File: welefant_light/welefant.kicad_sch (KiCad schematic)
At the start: 75 parts, among them J1 Conn_01x02, J2 Conn_02x8_Odd_Even, J3 Conn_02x11_Odd_Even, Q1 AO3401A, Q2 AO3401A, Q3 AO3401A, SW1 DPDT, SW2 RESET, SW3 BOOT, U1 NCP167BMX330TBG, U2 Audio Jack PJ-324, U3 GSA4737H12-F26-6P, U4 TP4056, U5 welefant, U6 ESP32-S3-WROOM-1(N16R2)

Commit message: blubb
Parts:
- removed D4: SS34, easyeda2kicad:SMA_L4.3-W2.6-LS5.2-RD, symbol easyeda2kicad:SS34_C8678
- removed R11: 2.4K, easyeda2kicad:R0603, symbol easyeda2kicad:0603WAF2401T5E
- added D4: 1N5819WS, Diode_SMD:D_SOD-323, symbol Diode:1N5819WS
- added R18: 10K, easyeda2kicad:R0603, symbol easyeda2kicad:0603WAF1002T5E
- added R19: 330, easyeda2kicad:R0603, symbol easyeda2kicad:0603WAF3300T5E
- BT1: value Battery_Cell -> Battery
- J1: footprint Connector_JST:JST_PH_B2B-PH-SM4-TB_1x02-1MP_P2.00mm_Vertical -> Connector_JST:JST_PH_B2B-PH-K_1x02_P2.00mm_Vertical
- J2, J3: footprint Connector_PinHeader_2.54mm:PinHeader_2x08_P2.54mm_Vertical_SMD -> hacrafu:PinHeader_2x08_P2.54mm_Vertical_SMD_handsolder
- SW1: footprint footprints:Switch_MSS22D18 -> hacrafu:Switch_MSS22D18
- U1: footprint easyeda2kicad:XDFN-4_L1.0-W1.0-P0.65-BL-EP -> hacrafu:XDFN-4
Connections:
- net BAT_SENS_EN: now also R18.2
- net GND: now also C11.2, SW2.4 (D), SW3.3 (C), U4.9 (EP)
- net V33: now also R18.1
- net V5: now also D4.2 (A)
- net VBUS: now also D4.1 (K)
- net at CLED1.1 (C): now also R19.1
- net at U4.7 (~{CHRG}): now also R19.2
- net RESET: now reaches C11.1, R17.2, SW2.2 (B), U6.3 (EN)
- net RESET: now also SW2.1 (A)
- net IO0: now reaches SW3.1 (A), U6.27 (IO0)
- net IO0: now also SW3.2 (B)
- no-connect marks 21 -> 17
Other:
- moved on the sheet: R16, SW3

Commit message: stand
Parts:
- BT1: footprint hacrafu:LiPo_Recycled -> hacrafu:LiPo_Recycled_welefant
- J3: value Conn_02x11_Odd_Even -> Conn_02x6_Odd_Even; footprint hacrafu:PinHeader_2x08_P2.54mm_Vertical_SMD_handsolder -> hacrafu:PinHeader_2x06_P2.54mm_Vertical_SMD_handsolder; symbol Connector_Generic:Conn_02x08_Odd_Even -> Connector_Generic:Conn_02x06_Odd_Even
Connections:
- net IO35: now also J3.5 (Pin_5); no longer J3.9 (Pin_9)
- net IO36: now also J3.6 (Pin_6); no longer J3.10 (Pin_10)
- net IO37: now also J3.7 (Pin_7); no longer J3.11 (Pin_11)
- net IO38: now also J3.8 (Pin_8); no longer J3.12 (Pin_12)
- net IO39: now also J3.9 (Pin_9); no longer J3.13 (Pin_13)
- net IO40: now also J3.10 (Pin_10); no longer J3.14 (Pin_14)
- net IO41: now also J3.11 (Pin_11); no longer J3.15 (Pin_15)
- net IO42: now also J3.12 (Pin_12); no longer J3.16 (Pin_16)
- net TOUCH_T4: no longer J3.5 (Pin_5)
- net TOUCH_T5: no longer J3.6 (Pin_6)
- net TOUCH_T6: no longer J3.7 (Pin_7)
- net IO21: no longer names the net of U6.23 (IO21)
- net IO21: no longer J3.8 (Pin_8)
- no-connect marks 17 -> 18
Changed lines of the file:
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@@
   (no_connect (at 183.515 38.1))
   (no_connect (at 27.94 25.4))
+  (no_connect (at 251.46 78.74))
   (no_connect (at 38.1 13.97))
   (no_connect (at 259.08 78.74))
@@
     (effects (font (size 1.27 1.27)) (justify right bottom))
   )
-  (label "IO21" (at 270.51 114.3 0) (fields_autoplaced)
-    (effects (font (size 1.27 1.27)) (justify left bottom))
-  )
   (label "LED_HEAD" (at 254 78.74 270) (fields_autoplaced)
     (effects (font (size 1.27 1.27)) (justify right bottom))
@@
     (effects (font (size 1.27 1.27)) (justify right bottom))
   )
-  (label "IO35" (at 257.81 116.84 180) (fields_autoplaced)
+  (label "IO35" (at 257.81 111.76 180) (fields_autoplaced)
     (effects (font (size 1.27 1.27)) (justify right bottom))
   )
@@
     (effects (font (size 1.27 1.27)) (justify right bottom))
   )
-  (label "TOUCH_T6" (at 257.81 114.3 180) (fields_autoplaced)
-    (effects (font (size 1.27 1.27)) (justify right bottom))
-  )
-  (label "IO36" (at 270.51 116.84 0) (fields_autoplaced)
+  (label "IO36" (at 270.51 111.76 0) (fields_autoplaced)
     (effects (font (size 1.27 1.27)) (justify left bottom))
   )
@@
     (effects (font (size 1.27 1.27)) (justify right bottom))
   )
-  (label "TOUCH_T4" (at 257.81 111.76 180) (fields_autoplaced)
-    (effects (font (size 1.27 1.27)) (justify right bottom))
-  )
   (label "TX" (at 220.345 109.22 0) (fields_autoplaced)
     (effects (font (size 1.27 1.27)) (justify left bottom))
@@
     (effects (font (size 1.27 1.27)) (justify left bottom))
   )
-  (label "IO38" (at 270.51 119.38 0) (fields_autoplaced)
+  (label "IO38" (at 270.51 114.3 0) (fields_autoplaced)
     (effects (font (size 1.27 1.27)) (justify left bottom))
   )
@@
     (effects (font (size 1.27 1.27)) (justify right bottom))
   )
-  (label "IO41" (at 257.81 124.46 180) (fields_autoplaced)
+  (label "IO41" (at 257.81 119.38 180) (fields_autoplaced)
     (effects (font (size 1.27 1.27)) (justify right bottom))
   )
@@
     (effects (font (size 1.27 1.27)) (justify right bottom))
   )
-  (label "IO39" (at 257.81 121.92 180) (fields_autoplaced)
-    (effects (font (size 1.27 1.27)) (justify right bottom))
-  )
-  (label "IO21" (at 251.46 78.74 270) (fields_autoplaced)
+  (label "IO39" (at 257.81 116.84 180) (fields_autoplaced)
     (effects (font (size 1.27 1.27)) (justify right bottom))
   )
@@
     (effects (font (size 1.27 1.27)) (justify left bottom))
   )
-  (label "IO42" (at 270.51 124.46 0) (fields_autoplaced)
+  (label "IO42" (at 270.51 119.38 0) (fields_autoplaced)
     (effects (font (size 1.27 1.27)) (justify left bottom))
   )
@@
     (effects (font (size 1.27 1.27)) (justify right bottom))
   )
-  (label "TOUCH_T5" (at 270.51 111.76 0) (fields_autoplaced)
-    (effects (font (size 1.27 1.27)) (justify left bottom))
-  )
   (label "VEXT" (at 49.53 152.4 0) (fields_autoplaced)
     (effects (font (size 1.27 1.27)) (justify left bottom))
@@
     (effects (font (size 1.27 1.27)) (justify right bottom))
   )
-  (label "IO40" (at 270.51 121.92 0) (fields_autoplaced)
+  (label "IO40" (at 270.51 116.84 0) (fields_autoplaced)
     (effects (font (size 1.27 1.27)) (justify left bottom))
   )
@@
     (effects (font (size 1.27 1.27)) (justify left bottom))
   )
-  (label "IO37" (at 257.81 119.38 180) (fields_autoplaced)
+  (label "IO37" (at 257.81 114.3 180) (fields_autoplaced)
     (effects (font (size 1.27 1.27)) (justify right bottom))
   )
@@
     )
   )
-  (symbol (lib_id "Connector_Generic:Conn_02x08_Odd_Even") (at 262.89 114.3 0) (unit 1)
+  (symbol (lib_id "Connector_Generic:Conn_02x06_Odd_Even") (at 262.89 111.76 0) (unit 1)
     (in_bom yes) (on_board yes) (dnp no)
-    (property "Reference" "J3" (at 264.795 100.33 0)
-      (effects (font (size 1.27 1.27)))
-    )
-    (property "Value" "Conn_02x11_Odd_Even" (at 264.16 102.87 0)
-      (effects (font (size 1.27 1.27)))
-    )
-    (property "Footprint" "hacrafu:PinHeader_2x08_P2.54mm_Vertical_SMD_handsolder" (at 262.89 114.3 0)
-      (effects (font (size 1.27 1.27)) hide)
-    )
-    (property "Datasheet" "~" (at 262.89 114.3 0)
+    (property "Reference" "J3" (at 264.795 100.965 0)
+      (effects (font (size 1.27 1.27)))
+    )
+    (property "Value" "Conn_02x6_Odd_Even" (at 264.16 102.87 0)
+      (effects (font (size 1.27 1.27)))
+    )
+    (property "Footprint" "hacrafu:PinHeader_2x06_P2.54mm_Vertical_SMD_handsolder" (at 262.89 111.76 0)
+      (effects (font (size 1.27 1.27)) hide)
+    )
+    (property "Datasheet" "~" (at 262.89 111.76 0)
       (effects (font (size 1.27 1.27)) hide)
     )
@@
     (pin "11")
     (pin "12")
-    (pin "13")
-    (pin "14")
-    (pin "15")
-    (pin "16")
     (pin "2")
     (pin "3")
@@
       (effects (font (size 1.27 1.27)) (justify left) hide)
     )
-    (property "Footprint" "hacrafu:LiPo_Recycled" (at 186.055 63.881 90)
-      (effects (font (size 1.27 1.27)) hide)
-    )
+    (property "Footprint" "hacrafu:LiPo_Recycled_welefant" (at 186.055 63.881 90)
+      (effects (font (size 1.27 1.27)) hide)
+    )

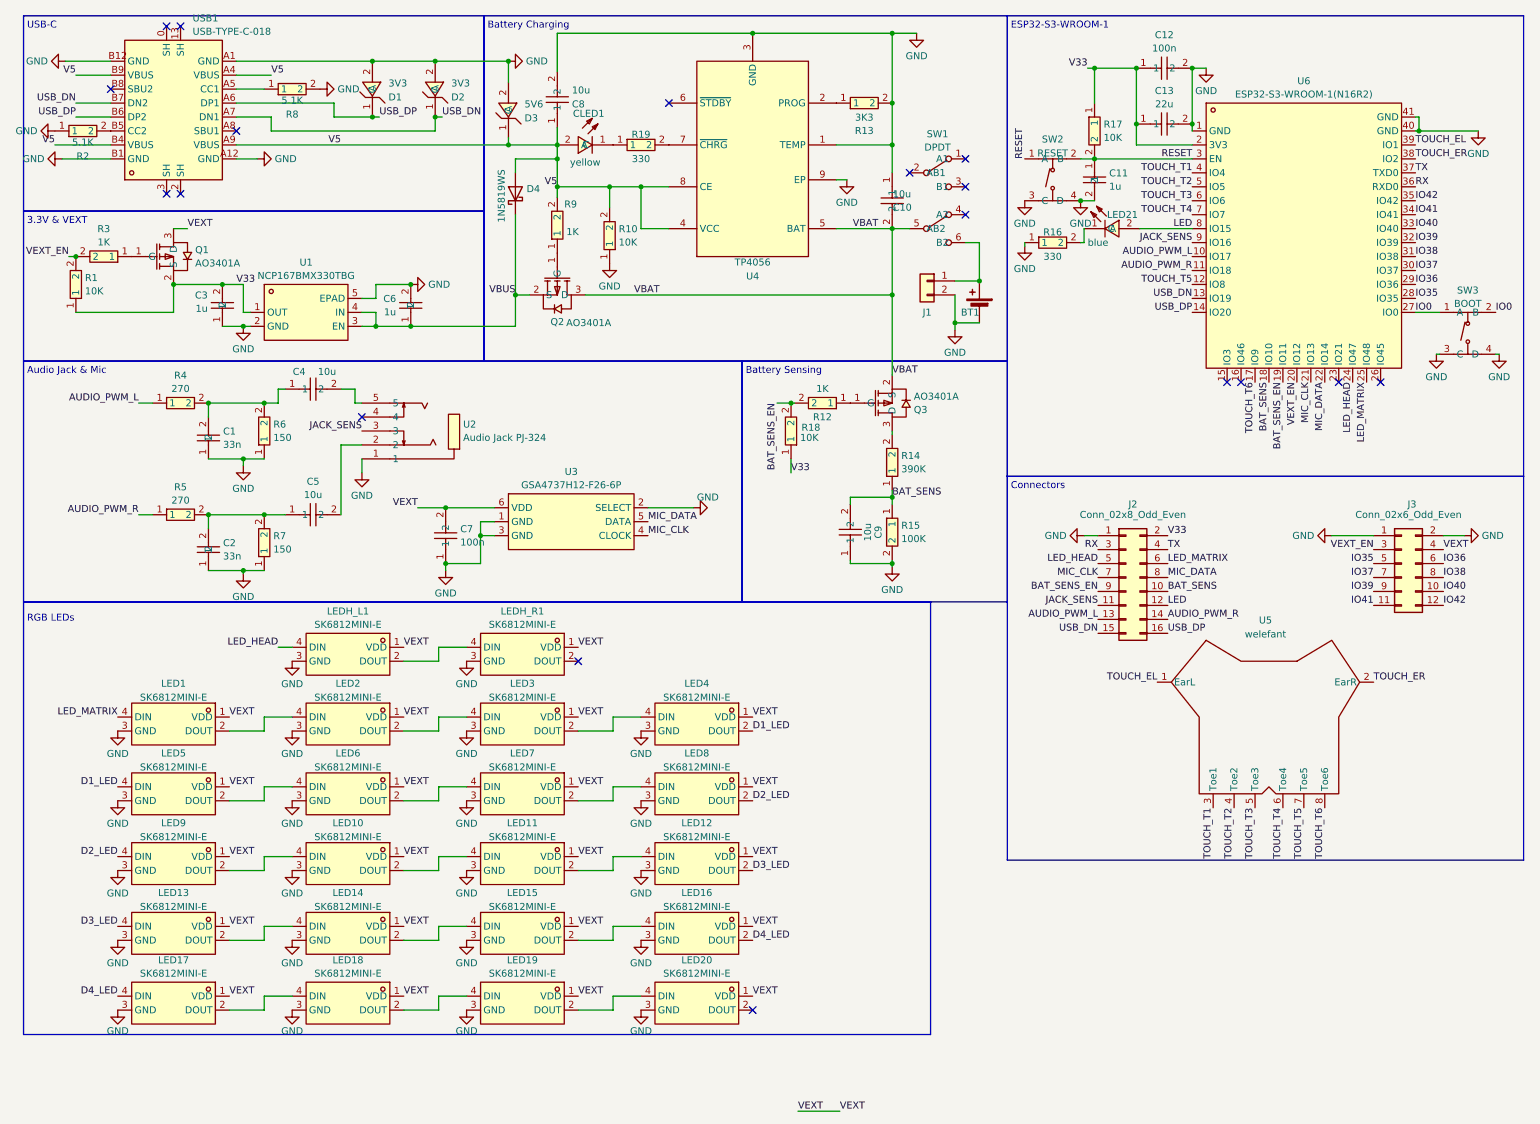
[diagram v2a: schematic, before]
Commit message: weiter welefant umgestaltung ohne wroom
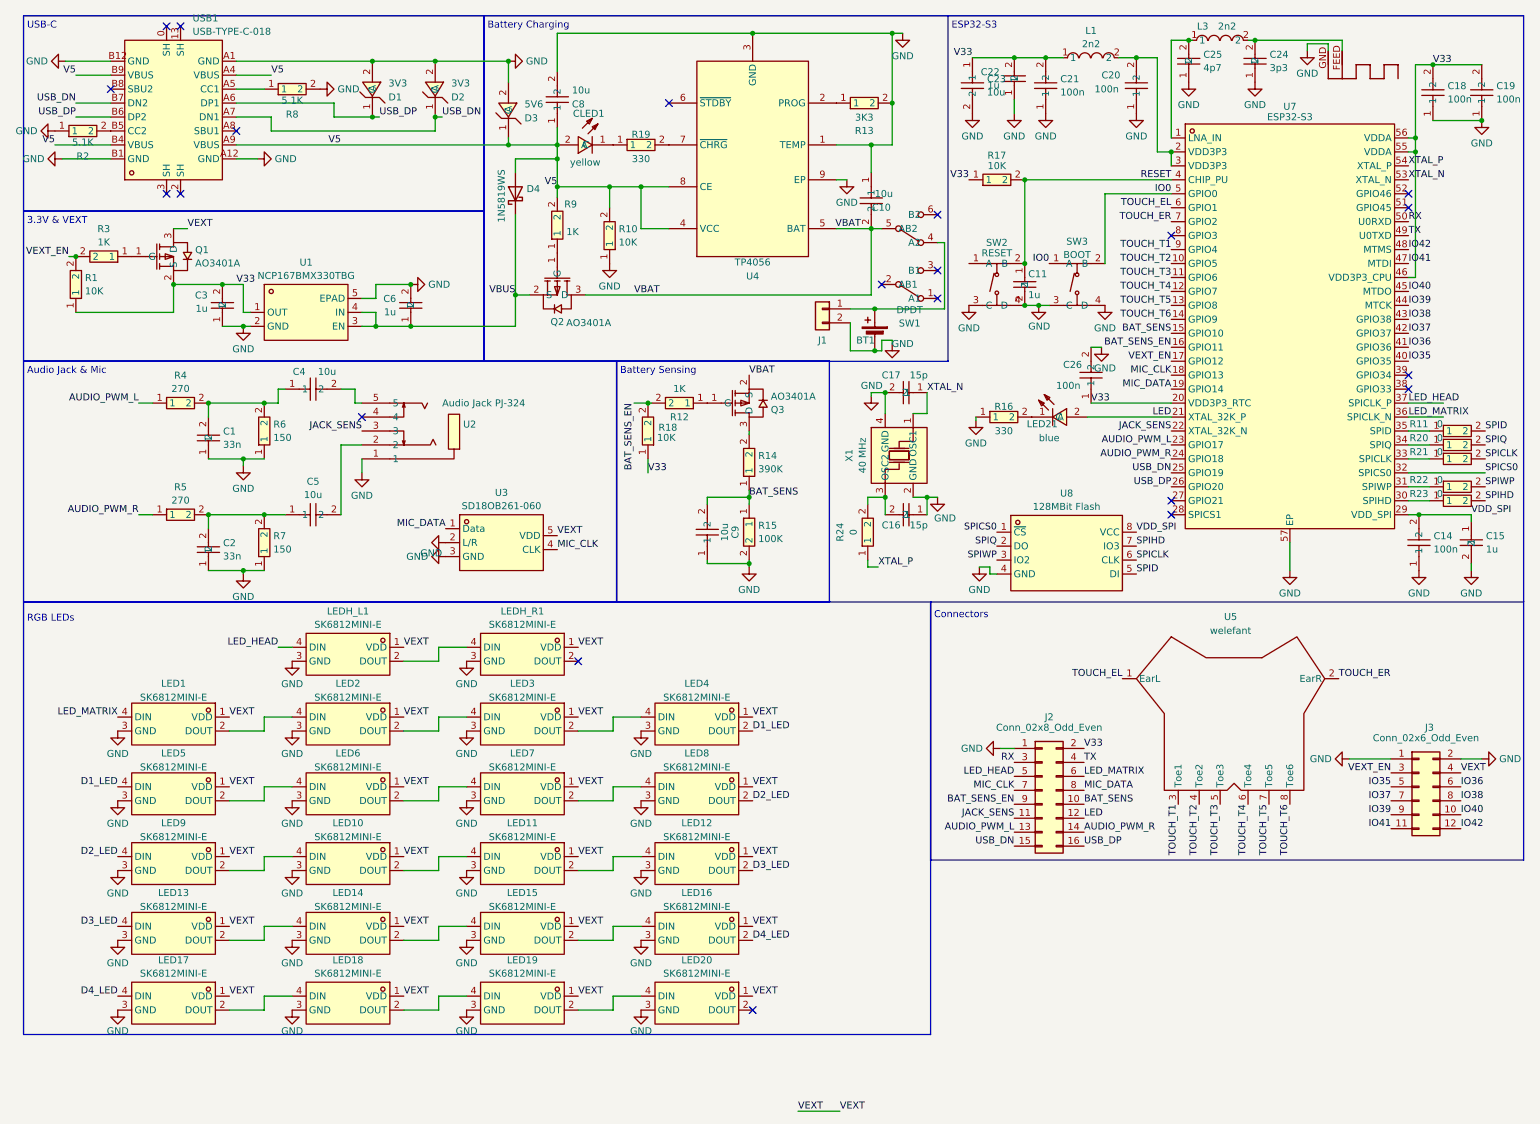
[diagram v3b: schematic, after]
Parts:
- removed C12, C7: 100n, easyeda2kicad:C0603, symbol easyeda2kicad:CC0603KRX7R9BB104
- removed C13: 22u, easyeda2kicad:C0603, symbol easyeda2kicad:CL10A226MQ8NRNC
- removed U3: GSA4737H12-F26-6P, easyeda2kicad:MIC-SMD_GSA4737H12-F26-6P, symbol easyeda2kicad:GSA4737H12-F26-6P
- removed U6: ESP32-S3-WROOM-1(N16R2), easyeda2kicad:WIRELM-SMD_ESP32-S3-WROOM-1, symbol easyeda2kicad:ESP32-S3-WROOM-1(N16R2)
- added ANT1: ANTENNA, hacrafu:antenna, symbol hacrafu:antenna
- added C14, C18, C19, C20, C21, C26: 100n, easyeda2kicad:C0603, symbol easyeda2kicad:CC0603KRX7R9BB104
- added C15, C22: 1u, easyeda2kicad:C0603, symbol easyeda2kicad:CL10A105KB8NNNC
- added C16, C17: 15p, easyeda2kicad:C0603, symbol easyeda2kicad:CL10C150JB8NNNC
- added C23: 10u, easyeda2kicad:C0603, symbol easyeda2kicad:CL10A106KP8NNNC
- added C24: 3p3, easyeda2kicad:C0402, symbol easyeda2kicad:0402CG3R3C500NT
- added C25: 4p7, easyeda2kicad:C0402, symbol easyeda2kicad:0402CG4R7C500NT
- added L1, L3: 2n2, easyeda2kicad:L0603, symbol easyeda2kicad:SDCL1608C2N2STDF
- added R11, R20, R21, R22, R23, R24: 0, easyeda2kicad:R0603, symbol easyeda2kicad:0603WAF0000T5E
- added U3: SD18OB261-060, easyeda2kicad:MIC-SMD_SD18OB261-060, symbol easyeda2kicad:SD18OB261-060
- added U7: ESP32-S3, easyeda2kicad:QFN-56_L7.0-W7.0-P0.40-TL-EP4.0, symbol easyeda2kicad:ESP32-S3
- added U8: 128MBit Flash, easyeda2kicad:SOIC-8_L5.3-W5.3-P1.27-LS8.0-BL, symbol easyeda2kicad:W25Q128JVSIQTR
- added X1: 40 MHz, easyeda2kicad:OSC-SMD_4P-L3.2-W2.5-BL_SIT8008BI, symbol easyeda2kicad:X322540MPB4SI
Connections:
- net AUDIO_PWM_L: now also U7.23 (GPIO17)
- net AUDIO_PWM_R: now also U7.24 (GPIO18)
- net BAT_SENS: now also U7.15 (GPIO10)
- net BAT_SENS_EN: now also U7.16 (GPIO11)
- net GND: now also ANT1.GND, C14.1, C15.2, C16.1, C17.2, C18.1, C19.1, C20.1, C21.1, C22.1, C23.2, C24.1, C25.1, C26.2, U3.2 (L/R), U3.3 (GND), U7.57 (EP), U8.4 (GND), X1.2 (GND), X1.4 (GND)
- net IO0: now also U7.5 (GPIO0)
- net IO35: now also U7.40 (GPIO35)
- net IO36: now also U7.41 (GPIO36)
- net IO37: now also U7.42 (GPIO37)
- net IO38: now also U7.43 (GPIO38)
- net IO39: now also U7.44 (MTCK)
- net IO40: now also U7.45 (MTDO)
- net IO41: now also U7.47 (MTDI)
- net IO42: now also U7.48 (MTMS)
- net JACK_SENS: now also U7.22 (XTAL_32K_N)
- net LED: now also U7.21 (XTAL_32K_P)
- net LED_HEAD: now also U7.37 (SPICLK_P)
- net LED_MATRIX: now also U7.36 (SPICLK_N)
- net MIC_CLK: now also U3.4 (CLK), U7.18 (GPIO13)
- net MIC_DATA: now also U3.1 (Data), U7.19 (GPIO14)
- net RESET: now also U7.4 (CHIP_PU); no longer SW2.1 (A)
- net RX: now also U7.50 (U0RXD)
- net TOUCH_EL: now also U7.6 (GPIO1)
- net TOUCH_ER: now also U7.7 (GPIO2)
- net TOUCH_T1: now also U7.9 (GPIO4)
- net TOUCH_T2: now also U7.10 (GPIO5)
- net TOUCH_T3: now also U7.11 (GPIO6)
- net TOUCH_T4: now also U7.12 (GPIO7)
- net TOUCH_T5: now also U7.13 (GPIO8)
- net TOUCH_T6: now also U7.14 (GPIO9)
- net TX: now also U7.49 (U0TXD)
- net USB_DN: now also U7.25 (GPIO19)
- net USB_DP: now also U7.26 (GPIO20)
- net V33: now also C18.2, C19.2, C21.2, C22.2, C23.1, C26.1, L1.1, U7.20 (VDD3P3_RTC), U7.46 (VDD3P3_CPU), U7.55 (VDDA), U7.56 (VDDA)
- net VEXT: now also U3.5 (VDD)
- net VEXT_EN: now also U7.17 (GPIO12)
- net at BT1.1 (+), J1.1 (Pin_1): now also SW1.4 (A2); no longer SW1.6 (B2)
- new net: C16.2, R24.2, X1.3 (OSC2)
- new net: R21.1, U7.33 (SPICLK)
- new net: C20.2, L1.2, U7.2 (VDD3P3), U7.3 (VDD3P3)
- new net: C25.2, L3.1, U7.1 (LNA_IN)
- new net: R23.1, U7.30 (SPIHD)
- new net: R22.1, U7.31 (SPIWP)
- new net: R20.1, U7.34 (SPIQ)
- new net: R11.1, U7.35 (SPID)
- new net: ANT1.FEED, C24.2, L3.2
- new net SPICLK: R21.2, U8.6 (CLK)
- new net SPICS0: U7.32 (SPICS0), U8.1 (~{CS})
- new net SPID: R11.2, U8.5 (DI)
- new net SPIHD: R23.2, U8.7 (IO3)
- new net SPIQ: R20.2, U8.2 (DO)
- new net SPIWP: R22.2, U8.3 (IO2)
- new net VDD_SPI: C14.2, C15.1, U7.29 (VDD_SPI), U8.8 (VCC)
- new net XTAL_N: C17.1, U7.53 (XTAL_N), X1.1 (OSC1)
- new net XTAL_P: R24.1, U7.54 (XTAL_P)
- no-connect marks 18 -> 21
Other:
- note added: "ESP32-S3"
- note removed: "ESP32-S3-WROOM-1"
- moved on the sheet: BT1, C10, C11, C9, J1, J2, J3, LED21, Q3, R12, R14, R15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

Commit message: weiter
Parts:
- removed C3: 1u, easyeda2kicad:C0603, symbol easyeda2kicad:CL10A105KB8NNNC
- removed SW1: DPDT, hacrafu:Switch_MSS22D18, symbol hacrafu:DPDT
- removed U1: NCP167BMX330TBG, hacrafu:XDFN-4, symbol easyeda2kicad:NCP167BMX330TBG
- added C3: 10u, easyeda2kicad:C0603, symbol easyeda2kicad:CL10A106KP8NNNC
- added R9: 100K, easyeda2kicad:R0603, symbol easyeda2kicad:0603WAF1003T5E
- added SW1: ON-OFF, easyeda2kicad:SW-SMD_MK-12C02-G025, symbol easyeda2kicad:MK-12C02-G025
- added SW4, SW5: GPIO33, easyeda2kicad:SW-SMD_4P-L5.1-W5.1-P3.70-LS6.5-TL-2, symbol easyeda2kicad:TS-1187A-B-A-B
- added U1: RT9080-33GJ5, easyeda2kicad:TSOT-23-5_L2.9-W1.6-P0.95-LS2.8-BL, symbol easyeda2kicad:RT9080-33GJ5
- added U8: Reset 2.8V, easyeda2kicad:SOT-23-3_L2.9-W1.6-P1.90-LS2.8-BR, symbol easyeda2kicad:VDD281MNTA
- LED21: symbol easyeda2kicad:19-217_BHC-ZL1M2RY_3T -> hacrafu:led_fixed
- renumbered C17 to C10, C16 to C11, C23 to C12, C22 to C13, C11 to C14, C21 to C15, C26 to C16, C20 to C17, C25 to C18, C24 to C19, C14 to C20, C18 to C21, C15 to C22, C19 to C23, C8 to C7, C9 to C8, C10 to C9, L3 to L2, R9 to R10, R10 to R11, R19 to R12, R18 to R13, R12 to R14, R14 to R15, R15 to R16, R13 to R17, R24 to R18, R17 to R19, R16 to R20, R11 to R21, R20 to R22, R21 to R23, R22 to R24, R23 to R25, U8 to U6
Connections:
- net GND: now also C6.1, C3.1, SW4.3 (C), SW4.4 (D), SW5.3 (C), SW5.4 (D), U1.2 (GND), U8.2 (VSS); no longer C6.2
- net RESET: now also SW2.1 (A), U8.1 (VOUT)
- net V33: now also C3.2, U1.5 (VOUT), U8.3 (VIN)
- net VBAT: now also BT1.1 (+), J1.1 (Pin_1)
- net VBUS: now also C6.2, R9.2, SW1.1, U1.1 (VIN); no longer C6.1, D4.1 (K), Q2.2 (S)
- net GPIO33: now reaches U7.38 (GPIO33)
- net GPIO33: now also SW4.1 (A), SW4.2 (B)
- net GPIO34: now reaches U7.39 (GPIO34)
- net GPIO34: now also SW5.1 (A), SW5.2 (B)
- new net: R9.1, U1.3 (EN)
- new net: D4.1 (K), Q2.2 (S), SW1.2
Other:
- moved on the sheet: C12, C13, C14, C15, C17, C6, C7, C9, CLED1, D3, D4, J1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
